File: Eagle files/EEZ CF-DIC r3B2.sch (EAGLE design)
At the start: 234 parts, among them IC1 MC79L05, IC2 LP2951, IC3 VIPer35L, IC4 SI8233BB-D-IS1, IC5 LM5041B, IC6 IR11688STRPBF, IC7 TL072, IC8 TL103W, IC9 TL431, P1 T910W-50K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

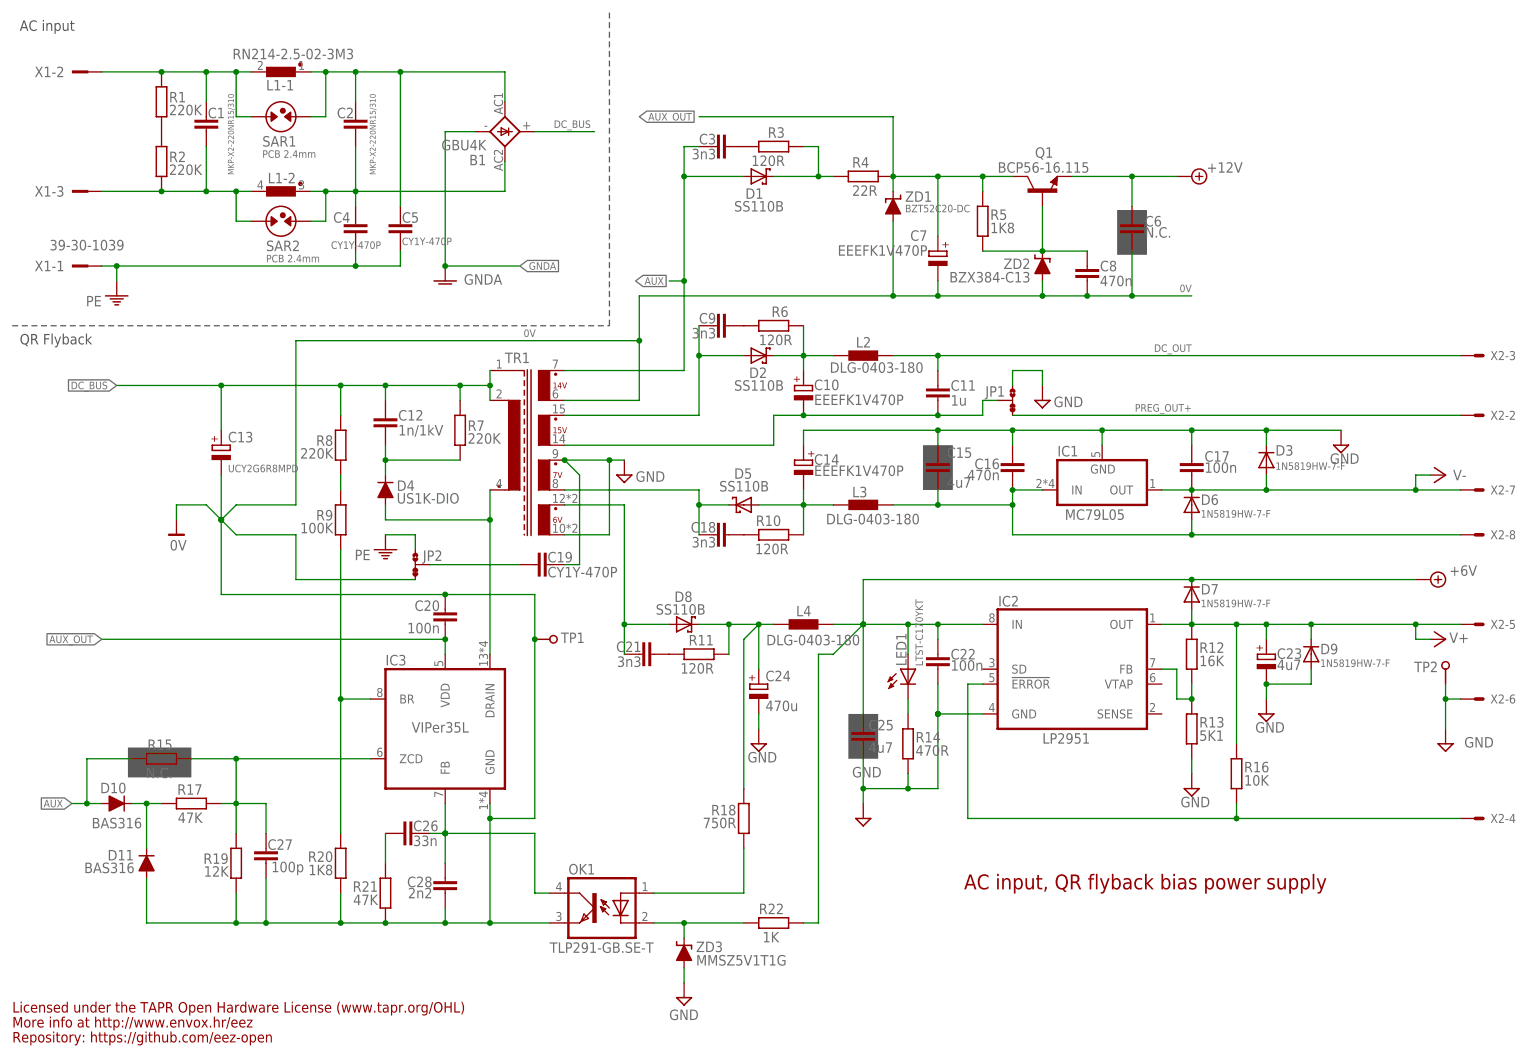
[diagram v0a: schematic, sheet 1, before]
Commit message: X2 12V connector added
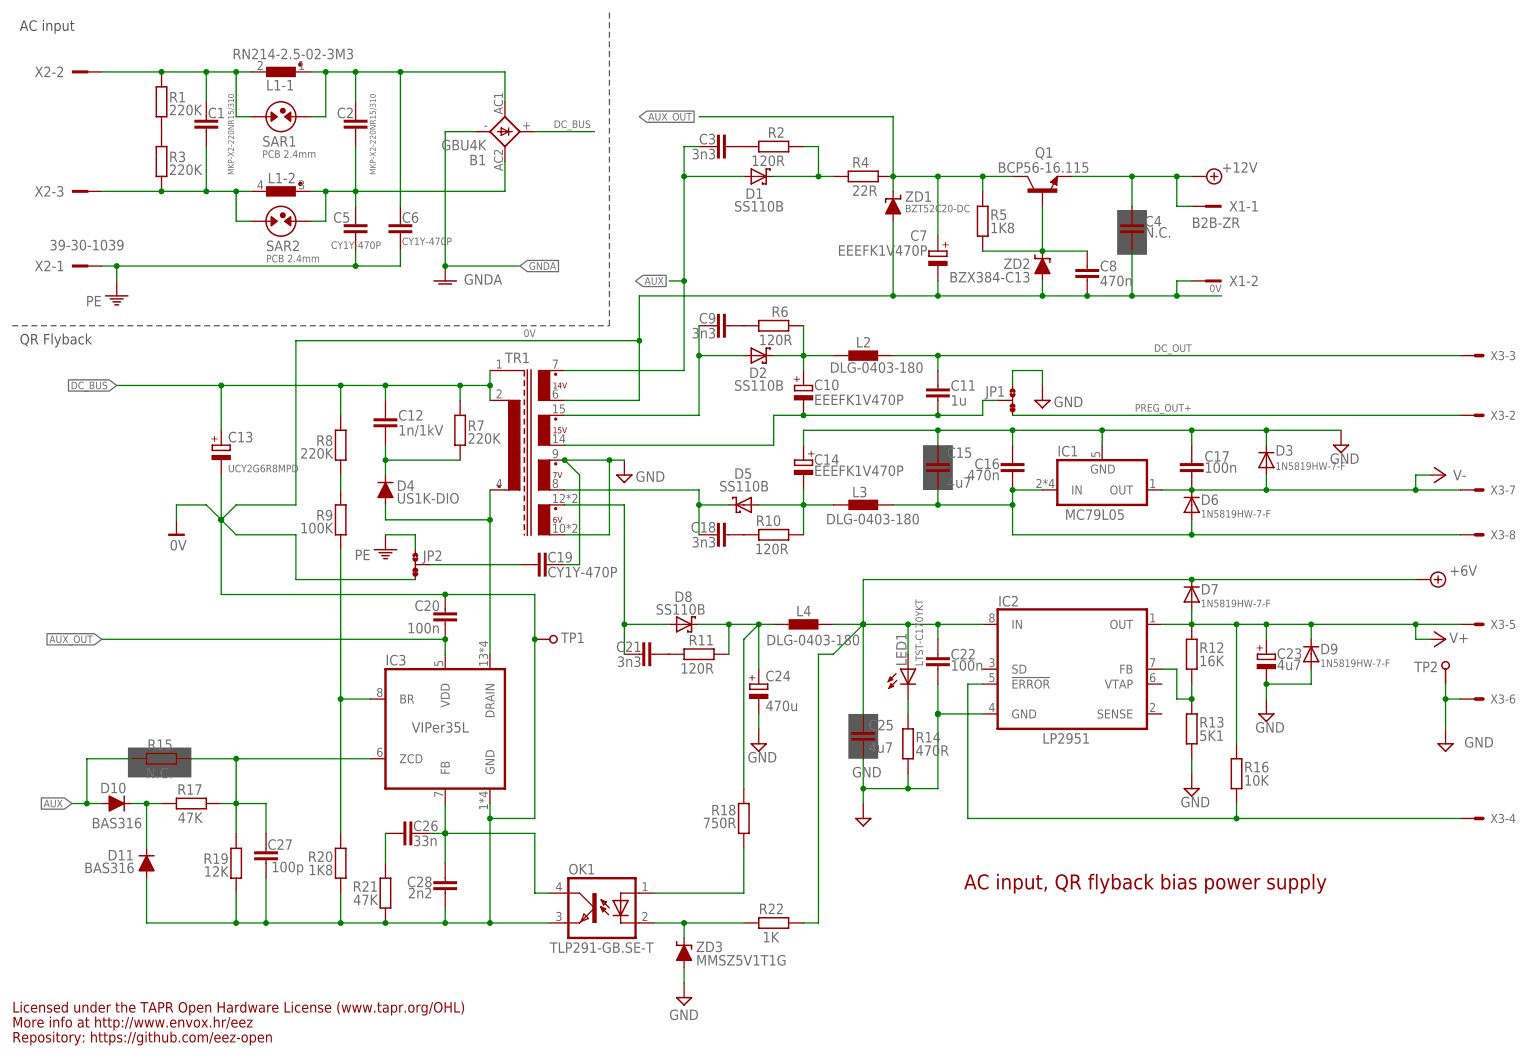
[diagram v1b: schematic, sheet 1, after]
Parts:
- added X4: 39-28-1023, EEZ_Lib1:MINIFIT_5566-02A
- C4: value CY1Y-470P -> N.C.; device EEZ_Lib1:C-EUCY -> rcl:C-EUC0603
- C6: value N.C. -> CY1Y-470P; device rcl:C-EUC0603 -> EEZ_Lib1:C-EUCY
- R2: value 220K -> 120R; device rcl:R-EU_R1206 -> rcl:R-EU_R0805
- R3: value 120R -> 220K; device rcl:R-EU_R0805 -> rcl:R-EU_R1206
- TP6: device EEZ_Lib1:TEST_POINT-2 -> EEZ_Lib1:PCB_TEST_TABSHIELD
- TP7: device EEZ_Lib1:PCB_TEST_TABSHIELD -> EEZ_Lib1:TEST_POINT-2
- X1: value 39-30-1039 -> B2B-ZR; device EEZ_Lib1:MINIFIT_39301039-CREEPAGE -> EEZ_Lib1:B2B-ZR
- X2: value 90136-1208 -> 39-30-1039; device con-molex:C-GRID-08-70543 -> EEZ_Lib1:MINIFIT_39301039-CREEPAGE
- X3: value 39-28-1023 -> 90136-1208; device EEZ_Lib1:MINIFIT_5566-02A -> con-molex:C-GRID-08-70543
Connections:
- net +12V: now also C4.1, X1-1.1; no longer C6.1
- net -9V: now also X3-8.S; no longer X2-8.S
- net 0V: now also C4.2, X1-2.1; no longer C6.2
- net DC_OUT: now also X3-3.S; no longer X2-3.S
- net FB: now also TP8.P$1; no longer TP7.P$1
- net GND: now also TP7.GND, X3-6.S, X4-2.1; no longer TP6.GND, X2-6.S, X3-2.1
- net ISO_FB: now also TP6.P$1; no longer TP8.P$1
- net N$140: now also R2.2; no longer R3.2
- net N$15: now also C6.2; no longer C5.2
- net N$24: now also C5.2; no longer C4.2
- net N$27: now also R2.1; no longer R3.1
- net N$28: now also X2-2.1; no longer X1-2.1
- net N$30: now also R3.2, X2-3.1; no longer R2.2, X1-3.1
- net N$33: now also R3.1; no longer R2.1
- net PE: now also C6.1, X2-1.1; no longer C4.1, X1-1.1
- net PREG_OUT+: now also TP7.TIP, X3-2.S, X4-1.1; no longer TP6.TIP, X2-2.S, X3-1.1
- net PWRGOOD: now also X3-4.S; no longer X2-4.S
- net U_MON: now also X3-1.S; no longer X2-1.S
- net V+: now also X3-5.S; no longer X2-5.S
- net V-: now also X3-7.S; no longer X2-7.S
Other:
- moved on the sheet: C4, C5, C6, R2, R3, X1-1, X1-2, X2-2, X2-3, X3-1

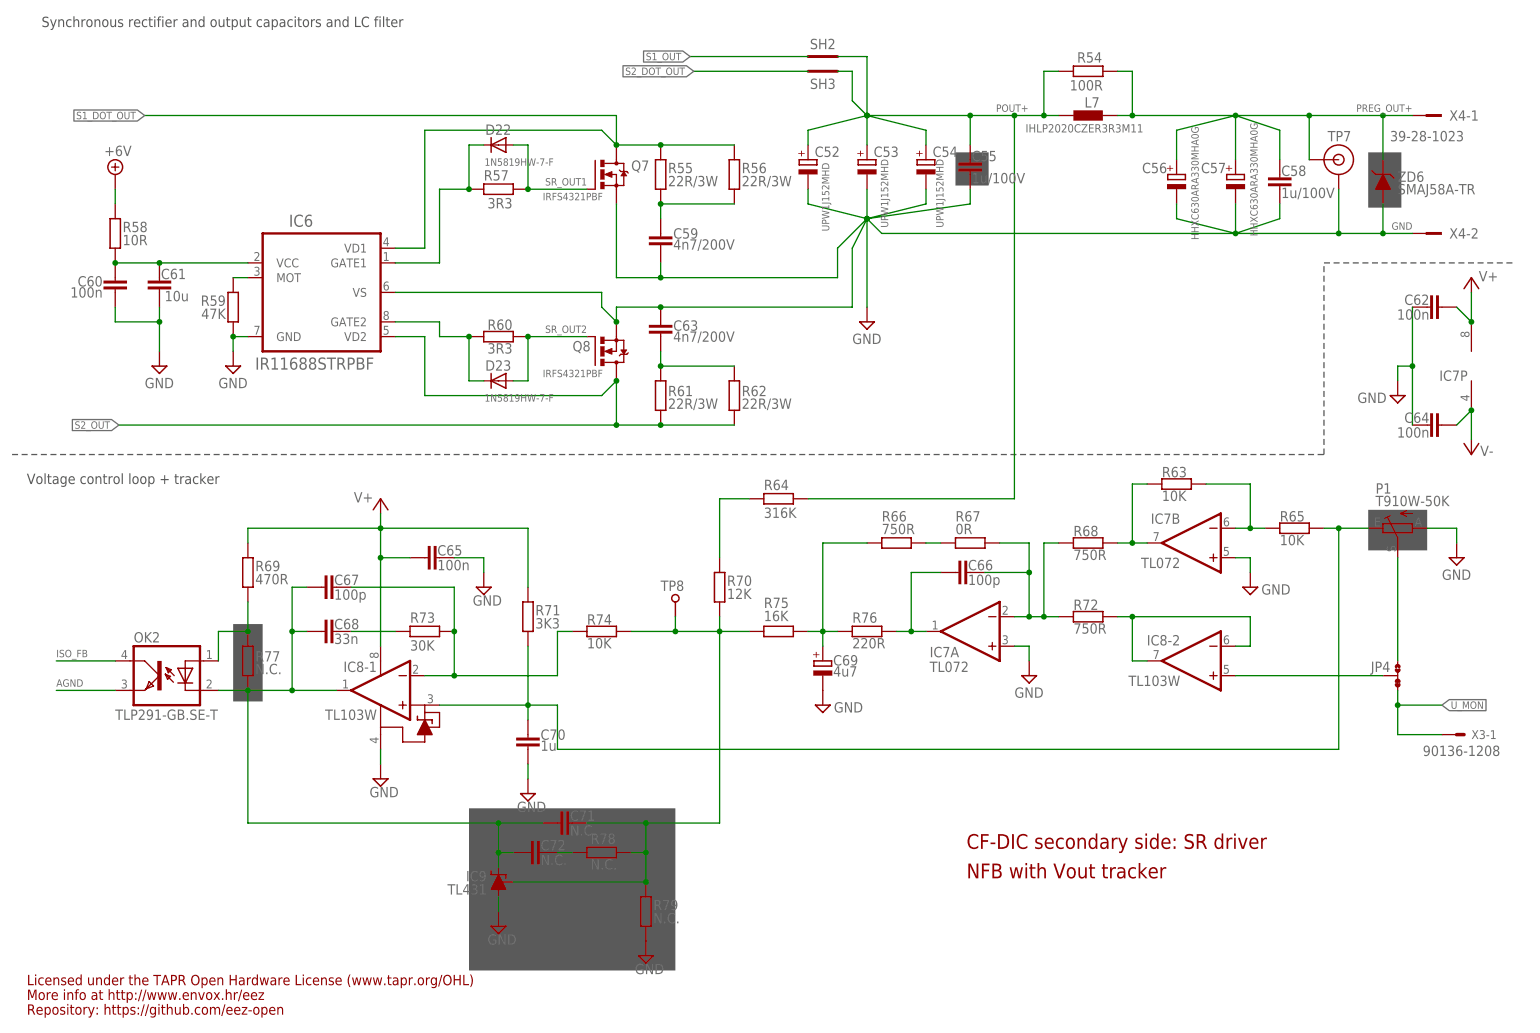
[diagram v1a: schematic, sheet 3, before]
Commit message: small changes on PCB, added alternative sync MOSFET in BOM
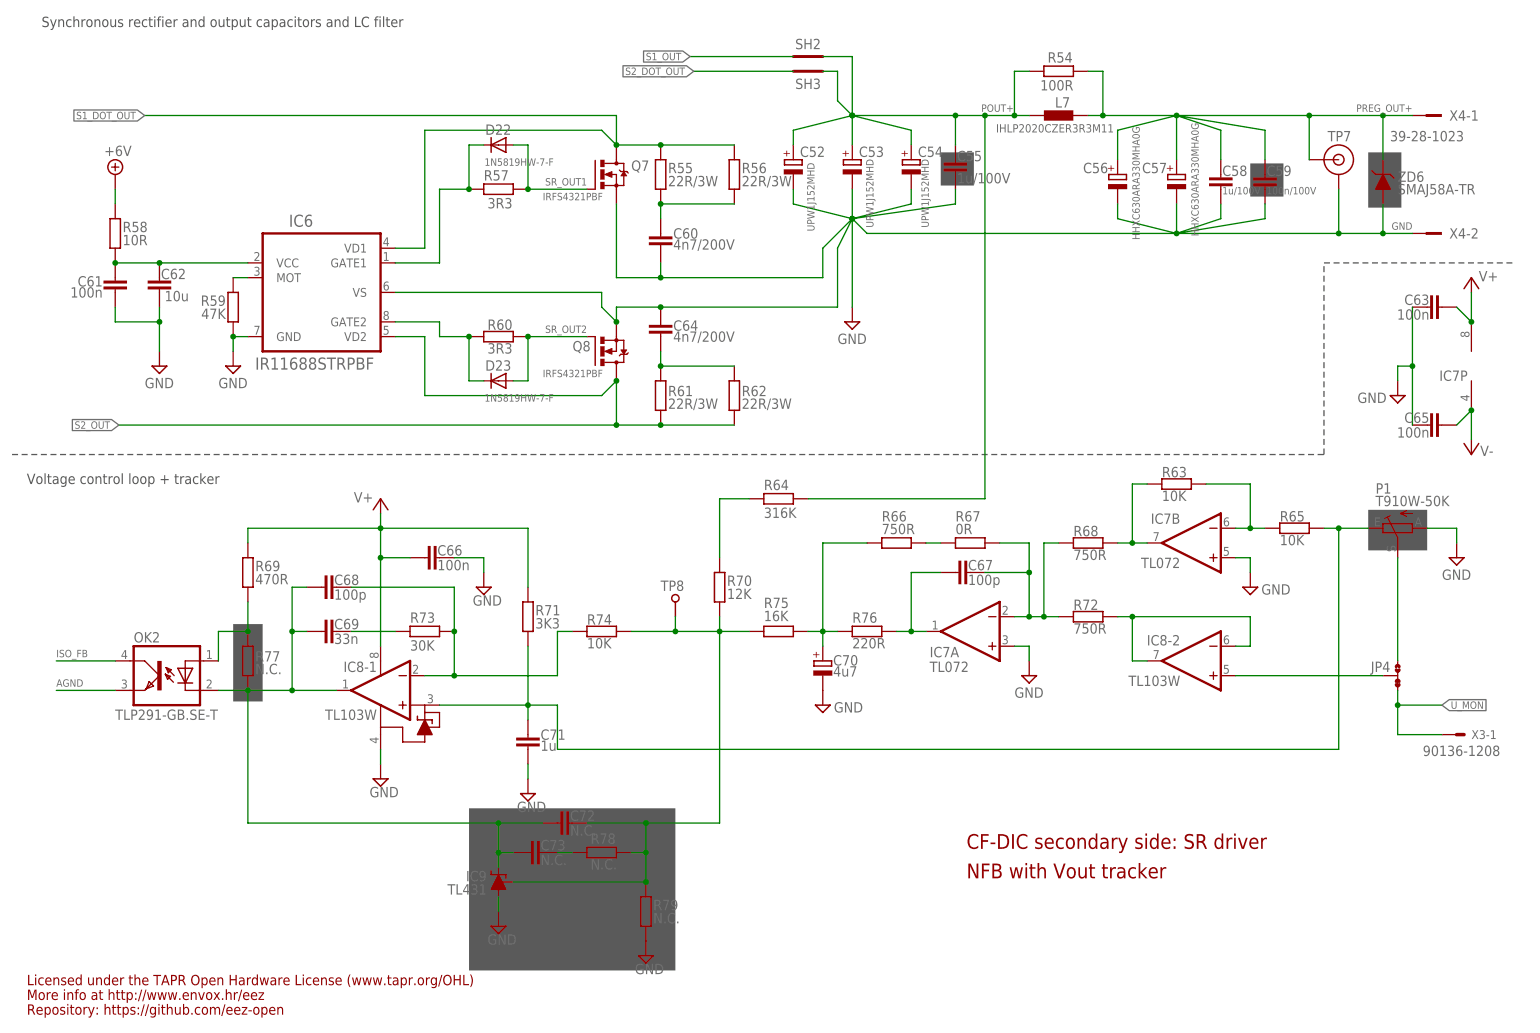
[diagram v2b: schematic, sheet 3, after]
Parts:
- added C73: N.C., rcl:C-EUC0805
- C59: value 4n7/200V -> 100n/100V; device rcl:C-EUC1206 -> rcl:C-EUC0805
- C60, C64: value 100n -> 4n7/200V; device rcl:C-EUC0603 -> rcl:C-EUC1206
- C61: value 10u -> 100n; device rcl:C-EUC1210 -> rcl:C-EUC0603
- C62: value 100n -> 10u; device rcl:C-EUC0603 -> rcl:C-EUC1210
- C63: value 4n7/200V -> 100n; device rcl:C-EUC1206 -> rcl:C-EUC0603
- C66: value 100p -> 100n; device rcl:C-EUC0805 -> rcl:C-EUC0603
- C68: value 33n -> 100p
- C69: value 4u7 -> 33n; device EEZ_Lib1:ECAP1206 -> rcl:C-EUC0805
- C70: value 1u -> 4u7; device rcl:C-EUC0805 -> EEZ_Lib1:ECAP1206
- C71: value N.C. -> 1u
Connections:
- net FB: now also C72.2; no longer C71.2
- net GND: now also C66.2, C70.-, C71.2; no longer C69.-, C70.2
- net N$1: now also C67.2; no longer C66.2
- net N$10: now also C68.2; no longer C67.2
- net N$134: now also C67.1; no longer C66.1
- net N$17: now also C73.2; no longer C72.2
- net N$6: now also C62.1; no longer C60.1
- net N$66: now also C60.1; no longer C59.1
- net N$67: now also C64.1; no longer C63.1
- net N$7: now also C71.1; no longer C70.1
- net N$76: now also C69.1, C73.1; no longer C67.1, C71.1
- net N$9: now also C69.2; no longer C68.2
- net NFB_OFFSET: now also C70.+; no longer C69.+
- net PREG_OUT+: now also C59.1
- net V+: now also C63.1, C66.1; no longer C62.1, C65.1
- net V-: now also C65.1; no longer C64.1
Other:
- moved on the sheet: C52, C53, C54, C55, C56, C57, C58, C59, C60, C61, C62, C63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
